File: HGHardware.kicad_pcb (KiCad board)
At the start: 2 copper layers, 220 x 60 mm, 109 parts, among them J1 Conn_01x04_Male, J2 SWD Conn, J3 USB_C_Receptacle_USB2.0, Q1 MMBTA42, Q2 FDS2672CT, SW1 SW_Push, SW2 SW_SPST, SW3 SW_Push, U1 STM32L433CBTx, U2 HV507PG-G-MyKiCadLib, U3 ESP-12S, U4 W25Q32FWSSIG, U5 UCC3803, U7 TXS0104EPWR, U9 AOZ1031, Y1 8MHz, Y2 8MHz

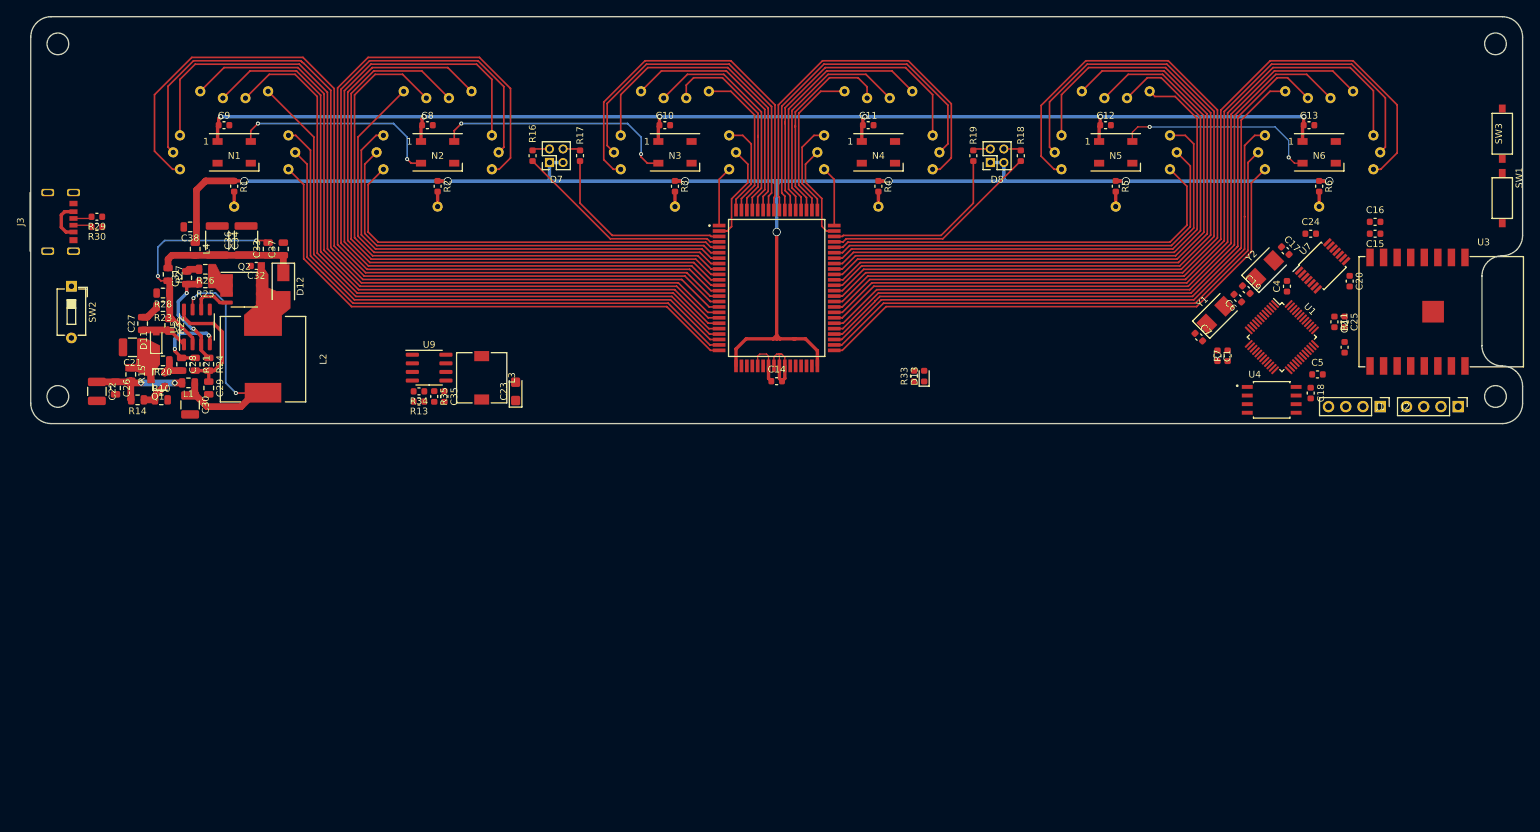
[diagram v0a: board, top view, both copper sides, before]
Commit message: 20210306完善原理图，升压模块将单独使用
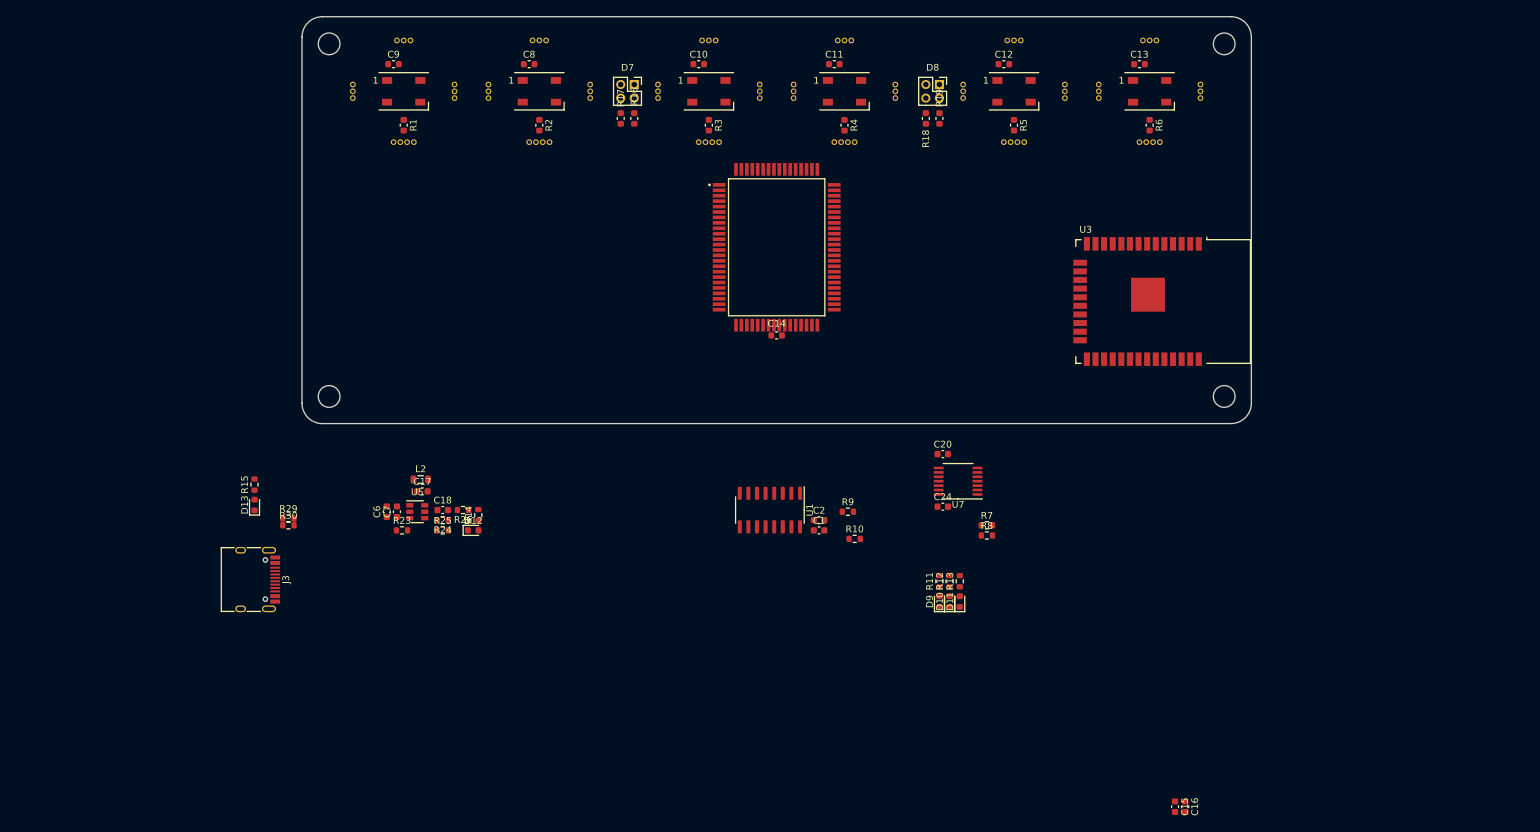
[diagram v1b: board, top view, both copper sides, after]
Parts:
- removed C19: 20pF, Capacitor_SMD:C_0603_1608Metric
- removed C21: 47uF 16v, Capacitor_SMD:C_1210_3225Metric
- removed C22, C30: 100uF 16v, Capacitor_SMD:C_1210_3225Metric
- removed C23: 10uF, Capacitor_Tantalum_SMD:CP_EIA-3216-18_Kemet-A
- removed C25, C35: 100nF, Capacitor_SMD:C_0603_1608Metric
- removed C26: 0.1uF, Capacitor_SMD:C_0805_2012Metric
- removed C27: 220pF, Capacitor_SMD:C_0805_2012Metric
- removed C28: 430pF, Capacitor_SMD:C_0805_2012Metric
- removed C29: 0.1uF 16v, Capacitor_SMD:C_0805_2012Metric
- removed C31: 1nF, Capacitor_SMD:C_0805_2012Metric
- removed C32: 560pF 250v, Capacitor_SMD:C_0603_1608Metric
- removed C33: 100pF 250v, Capacitor_SMD:C_0805_2012Metric
- removed C34, C36: 1uF 250v, Capacitor_SMD:C_1812_4532Metric
- removed C37, C38: 0.1uF 250v, Capacitor_SMD:C_0805_2012Metric
- removed C4, C5: C, Capacitor_SMD:C_0603_1608Metric
- removed J1: Conn_01x04_Male, Connector_PinHeader_2.54mm:PinHeader_1x04_P2.54mm_Vertical
- removed J2: SWD Conn, Connector_PinHeader_2.54mm:PinHeader_1x04_P2.54mm_Vertical
- removed L1, L4: 60ohm 100Mhz, Resistor_SMD:R_0805_2012Metric
- removed L3: 4.7uH, Inductor_SMD:L_7.3x7.3_H3.5
- removed Q1: MMBTA42, Package_TO_SOT_SMD:SOT-23
- removed Q2: FDS2672CT, Package_SO:SO-8_3.9x4.9mm_P1.27mm
- removed R20: 100k, Resistor_SMD:R_0805_2012Metric
- removed R21: 60.4k, Resistor_SMD:R_0805_2012Metric
- removed R22: N.U., Resistor_SMD:R_0805_2012Metric
- removed R27: 634k, Resistor_SMD:R_0805_2012Metric
- removed R28: 7.68k, Resistor_SMD:R_0805_2012Metric
- removed R33: 1KO, Resistor_SMD:R_0603_1608Metric
- removed R34: 10KO, Resistor_SMD:R_0603_1608Metric
- removed R35: 1.5KO, Resistor_SMD:R_0603_1608Metric
- removed SW1, SW3: SW_Push, HGHardware:MyButton
- removed SW2: SW_SPST, Button_Switch_THT:SW_DIP_SPSTx01_Slide_6.7x4.1mm_W7.62mm_P2.54mm_LowProfile
- removed U4: W25Q32FWSSIG, SOIC127P790X216-8N:SOIC127P790X216-8N
- removed U9: AOZ1031, Package_SO:SOIC-8_3.9x4.9mm_P1.27mm
- removed Y1, Y2: 8MHz, Crystal:Crystal_SMD_5032-2Pin_5.0x3.2mm
- added D10: BLUE, LED_SMD:LED_0603_1608Metric, F.Cu at (105.5, 66.2)
- added D9: GREEN, LED_SMD:LED_0603_1608Metric, F.Cu at (104.0, 66.2)
- added R12: 1KΩ, Resistor_SMD:R_0603_1608Metric, F.Cu at (105.5, 63.2)
- added R8: 120Ω, Resistor_SMD:R_0603_1608Metric, F.Cu at (111.0, 56.5)
- added R9: 10KΩ, Resistor_SMD:R_0603_1608Metric, F.Cu at (90.5, 53.0)
- C1: value 100nF -> 10uF
- C15: value 10uF -> 100uF
- C17, C7: value 20pF -> 100nF
- C18: value 100nF -> 22uF
- C2: value C -> 100nF
- C6: value 20pF -> 22uF
- D1: value WS2812C -> WS2812B×6
- D11: value BAT54 -> RED; footprint Diode_SMD:D_SOD-323_HandSoldering -> LED_SMD:LED_0603_1608Metric
- D12: value ES1D -> RED; footprint Diode_SMD:D_SMA -> LED_SMD:LED_0603_1608Metric
- D13: value LED -> RED
- D2, D3: value WS2812C -> WS2812B-2020
- J3: footprint HGHardware:USB TypeC 6P Horizontal -> Connector_USB:USB_C_Receptacle_HRO_TYPE-C-31-M-12
- L2: value 33uH -> 2.2uH; footprint Inductor_SMD:L_12x12mm_H4.5mm -> Inductor_SMD:L_0805_2012Metric
- N6: value NixieTube -> NixieTube×6
- R1, R2, R3, R4, R5, R6: value 33KO -> 33KΩ
- R10, R25: value 1k -> 10KΩ; footprint Resistor_SMD:R_0805_2012Metric -> Resistor_SMD:R_0603_1608Metric
- R11: value 10KO -> 1KΩ
- R13: value 31.1KO -> 1KΩ
- R14: value 100k -> 1KΩ; footprint Resistor_SMD:R_0805_2012Metric -> Resistor_SMD:R_0603_1608Metric
- R15: value 2k -> 1KΩ; footprint Resistor_SMD:R_0805_2012Metric -> Resistor_SMD:R_0603_1608Metric
- R17: value 510KO -> 510KΩ
- R23: value 0 Ohm -> 100KΩ; footprint Resistor_SMD:R_0805_2012Metric -> Resistor_SMD:R_0603_1608Metric
- R24: value 4.12k -> 30KΩ; footprint Resistor_SMD:R_0805_2012Metric -> Resistor_SMD:R_0603_1608Metric
- R26: value 0.1 1/2W -> 0Ω; footprint Resistor_SMD:R_0805_2012Metric -> Resistor_SMD:R_0603_1608Metric
- R29, R30: value 5.1K -> 5.1KΩ
- R7: value 10KO -> 120Ω
- U1: value STM32L433CBTx -> CH340C; footprint Package_QFP:LQFP-48_7x7mm_P0.5mm -> Package_SO:SOIC-16_3.9x9.9mm_P1.27mm
- U2: value HV507PG-G-MyKiCadLib -> HV507PG-G
- U3: value ESP-12S -> ESP32-WROOM-32; footprint ESP-12S:ESP-12S -> RF_Module:ESP32-WROOM-32
- U5: value UCC3803 -> TPS563201DDCR; footprint Package_SO:SO-8_3.9x4.9mm_P1.27mm -> Package_TO_SOT_SMD:SOT-23-6
- moved C17 132.1 mm to (27.8, 50.0), turned to 0 degrees
- moved C6 129.4 mm to (22.5, 53.0), turned to 90 degrees
- moved C18 129.2 mm to (30.8, 52.8), turned to 0 degrees
- moved D11 124.6 mm to (107.0, 66.2)
- moved C7 121.0 mm to (24.0, 53.0), turned to 90 degrees
- moved R10 104.3 mm to (91.5, 57.0)
- moved D13 100.6 mm to (3.00, 52.0)
- moved C16 90.7 mm to (140.2, 96.5), turned to 270 degrees
- moved C15 89.5 mm to (138.8, 96.5), turned to 270 degrees
- moved R13 84.0 mm to (107.0, 63.2), turned to 90 degrees
- moved C2 81.6 mm to (86.2, 54.2), turned to 0 degrees
- moved U1 79.7 mm to (79.0, 52.8), turned to 270 degrees
- moved R11 69.7 mm to (104.0, 63.2), turned to 90 degrees
- moved C24 67.6 mm to (104.5, 52.2), turned to 0 degrees
- moved C20 65.2 mm to (104.5, 44.5), turned to 0 degrees
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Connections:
- C1 pad 1: /NRST -> +3V3
- C1 pad 2: GND -> GNDD
- C10 pad 2: GND -> GNDD
- C11 pad 2: GND -> GNDD
- C12 pad 2: GND -> GNDD
- C13 pad 2: GND -> GNDD
- C14 pad 1: GND -> GNDD
- C15 pad 2: GND -> GNDD
- C16 pad 2: GND -> GNDD
- C17 pad 2: GND -> Net-(C17-Pad2)
- C18 pad 1: GND -> GNDD
- C18 pad 2: +3V3 -> Net-(C18-Pad2)
- C2 pad 2: GND -> GNDD
- C20 pad 2: GND -> GNDD
- C24 pad 2: GND -> GNDD
- C6 pad 1: Net-(C6-Pad1) -> +5V
- C7 pad 1: Net-(C7-Pad1) -> +5V
- C8 pad 2: GND -> GNDD
- C9 pad 2: GND -> GNDD
- D1 pad 3: GND -> GNDD
- D11 pad 1: Net-(C21-Pad1) -> Net-(D11-Pad1)
- D11 pad 2: Net-(C27-Pad1) -> Net-(D11-Pad2)
- D12 pad 1: Net-(C33-Pad1) -> GNDD
- D12 pad 2: Net-(C32-Pad1) -> Net-(D12-Pad2)
- D13 pad 1: Net-(D13-Pad1) -> GNDD
- D2 pad 3: GND -> GNDD
- D3 pad 3: GND -> GNDD
- D4 pad 3: GND -> GNDD
- D5 pad 3: GND -> GNDD
- D6 pad 2: (no net) -> Net-(D6-Pad2)
- D6 pad 3: GND -> GNDD
- L2 pad 1: Net-(C32-Pad1) -> Net-(C17-Pad1)
- L2 pad 2: Net-(C30-Pad1) -> Net-(C18-Pad2)
- R10 pad 1: Net-(Q1-Pad1) -> Net-(Q3-Pad2)
- R10 pad 2: /VPP_EN -> Net-(Q1-Pad1)
- R11 pad 1: /BOOT0 -> Net-(D9-Pad2)
- R11 pad 2: GND -> +3V3
- R13 pad 1: +3V3 -> Net-(D11-Pad2)
- R13 pad 2: Net-(R13-Pad2) -> +3V3
- R14 pad 1: Net-(Q1-Pad1) -> Net-(D12-Pad2)
- R14 pad 2: +5V -> +3V3
- R15 pad 1: Net-(C21-Pad1) -> Net-(D13-Pad2)
- R23 pad 1: Net-(C33-Pad2) -> +5V
- R23 pad 2: Net-(C27-Pad2) -> Net-(R23-Pad2)
- R24 pad 1: Net-(C31-Pad1) -> Net-(C18-Pad2)
- R24 pad 2: Net-(C29-Pad1) -> Net-(R24-Pad2)
- R25 pad 1: Net-(Q2-Pad1) -> Net-(R24-Pad2)
- R25 pad 2: Net-(C31-Pad1) -> GND
- R26 pad 1: Net-(Q2-Pad1) -> +3V3
- R26 pad 2: GND -> Net-(C18-Pad2)
- R7 pad 1: /NRST -> /CH340_TXD
- R7 pad 2: +3V3 -> Net-(R7-Pad2)
- U1 pad 1: +3V3 -> GNDD
- U1 pad 10: /WKP1 -> Net-(U1-Pad10)
- U1 pad 11: Net-(D13-Pad1) -> Net-(U1-Pad11)
- U1 pad 12: (no net) -> Net-(U1-Pad12)
- U1 pad 13: /VPP_EN -> Net-(Q3-Pad1)
- U1 pad 14: (no net) -> Net-(Q1-Pad1)
- U1 pad 15: (no net) -> Net-(U1-Pad15)
- U1 pad 16: /QSPI_IO3 -> +3V3
- U1 pad 2: (no net) -> Net-(R7-Pad2)
- U1 pad 3: Net-(C17-Pad1) -> Net-(R8-Pad2)
- U1 pad 4: Net-(C19-Pad1) -> +3V3
- U1 pad 5: Net-(C6-Pad1) -> /USB_D+
- U1 pad 6: Net-(C7-Pad1) -> /USB_D-
- U1 pad 7: /NRST -> Net-(U1-Pad7)
- U1 pad 8: GND -> Net-(U1-Pad8)
- U1 pad 9: +3V3 -> Net-(U1-Pad9)
- U2 pad 30: GND -> GNDD
- U2 pad 32: GND -> GNDD
- U2 pad 33: GND -> GNDD
- U2 pad 39: (no net) -> Net-(U2-Pad39)
- U3 pad 1: (no net) -> GNDD
- U3 pad 10: (no net) -> Net-(U3-Pad10)
- U3 pad 11: (no net) -> Net-(U3-Pad11)
- U3 pad 12: (no net) -> Net-(U3-Pad12)
- U3 pad 13: (no net) -> Net-(U3-Pad13)
- U3 pad 14: (no net) -> Net-(U3-Pad14)
- U3 pad 15: /UART1_TX -> GNDD
- U3 pad 16: /UART1_RX -> Net-(U3-Pad16)
- U3 pad 2: (no net) -> +3V3
- U3 pad 3: (no net) -> /ESP32_EN
- U3 pad 4: (no net) -> Net-(U3-Pad4)
- U3 pad 5: /WKP1 -> Net-(U3-Pad5)
- U3 pad 6: /NRST -> Net-(U3-Pad6)
- U3 pad 7: /BOOT0 -> Net-(U3-Pad7)
- U3 pad 8: +3V3 -> Net-(U3-Pad8)
- U3 pad 9: GND -> Net-(U3-Pad9)
- U5 pad 1: Net-(C27-Pad1) -> GND
- U5 pad 2: Net-(C33-Pad2) -> Net-(C17-Pad1)
- U5 pad 3: Net-(C31-Pad1) -> +5V
- U5 pad 4: Net-(C28-Pad1) -> Net-(R24-Pad2)
- U5 pad 5: GND -> Net-(R23-Pad2)
- U5 pad 6: Net-(Q2-Pad4) -> Net-(C17-Pad2)
- U7 pad 6: (no net) -> Net-(U7-Pad6)
- U7 pad 7: GND -> GNDD
- U7 pad 9: (no net) -> Net-(U7-Pad9)
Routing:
- net VPP: track 238.1 -> 0.00 mm, vias 7 -> 0
- net +5V: track 205.2 -> 0.00 mm, vias 8 -> 0
- net /N10: track 127.2 -> 0.00 mm
- net /N21: track 125.5 -> 0.00 mm
- net /N61: track 123.1 -> 0.00 mm
- net /N50: track 121.9 -> 0.00 mm
- net /N19: track 121.5 -> 0.00 mm
- net /N22: track 118.7 -> 0.00 mm
- net /N62: track 117.7 -> 0.00 mm
- net /N18: track 117.4 -> 0.00 mm
- net /N59: track 115.0 -> 0.00 mm
- net /N63: track 113.6 -> 0.00 mm
- net /N23: track 112.7 -> 0.00 mm
- net /N58: track 109.0 -> 0.00 mm
- net /N17: track 106.8 -> 0.00 mm
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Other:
- board size 220 x 60 mm -> 140 x 60 mm

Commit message: 犹豫不决ing
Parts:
- removed the C10 at (68.5, -13.0)
- removed the C15 at (138.8, 96.5)
- removed the C6 at (22.5, 53.0)
- removed the D6 at (25.0, -9.00)
- removed L2: 2.2uH, Inductor_SMD:L_0805_2012Metric
- removed the R1 at (25.0, -4.00)
- removed the R23 at (24.8, 55.8)
- removed the R26 at (33.8, 52.8)
- removed R30: 5.1KΩ, Resistor_SMD:R_0603_1608Metric
- added C1: 100uF, Capacitor_SMD:C_0603_1608Metric, F.Cu at (108.3, 73.3)
- added C13: 10uF, Capacitor_SMD:C_0603_1608Metric, F.Cu at (134.5, 56.1)
- added C14: 100nF, Capacitor_SMD:C_0603_1608Metric, F.Cu at (136.0, 56.1)
- added C2: 100nF, Capacitor_SMD:C_0603_1608Metric, F.Cu at (109.8, 73.3)
- added C3: 22uF, Capacitor_SMD:C_0603_1608Metric, F.Cu at (11.8, 28.7)
- added C4: 100nF, Capacitor_SMD:C_0603_1608Metric, F.Cu at (11.8, 30.2)
- added C8: C, Capacitor_SMD:C_0603_1608Metric, F.Cu at (58.2, 26.6)
- added D13: WS2812C, LED_SMD:LED_WS2812B_PLCC4_5.0x5.0mm_P3.2mm, F.Cu at (30.0, -9.00)
- added J1: USB_C_Receptacle_USB2.0, Connector_USB:USB_C_Receptacle_HRO_TYPE-C-31-M-12, F.Cu at (13.0, 14.9)
- added L1: 2.2uH, Inductor_SMD:L_Taiyo-Yuden_MD-4040, F.Cu at (16.3, 24.2)
- added Q1: S8050, Package_TO_SOT_SMD:SOT-23, F.Cu at (30.3, 15.7)
- added Q2: S8050, Package_TO_SOT_SMD:SOT-23, F.Cu at (30.3, 24.4)
- added Q3: S8050, Package_TO_SOT_SMD:SOT-23, F.Cu at (30.3, 20.9)
- added R13: 10KΩ, Resistor_SMD:R_0603_1608Metric, F.Cu at (28.5, 18.3)
- added R2: 5.1KΩ, Resistor_SMD:R_0603_1608Metric, F.Cu at (15.5, 21.1)
- added R22: 33KΩ, Resistor_SMD:R_0603_1608Metric, F.Cu at (70.2, -18.0)
- added R4: NC, Resistor_SMD:R_0603_1608Metric, F.Cu at (60.3, 28.9)
- added R9: 33KΩ, Resistor_SMD:R_0603_1608Metric, F.Cu at (29.2, -18.0)
- added U6: HV507PG-G, HGHardware:QFP80P2390X1790X340-80N, F.Cu at (80.0, 12.0)
- added Y1: 32.738kHz, Crystal:Crystal_SMD_2012-2Pin_2.0x1.2mm, F.Cu at (60.3, 27.2)
- C16, C17, C7: value 100nF -> C
- C9: value C -> 100nF
- J3: value USB_C_Receptacle_USB2.0 -> Conn_01x06; footprint Connector_USB:USB_C_Receptacle_HRO_TYPE-C-31-M-12 -> Connector_PinHeader_2.54mm:PinHeader_1x06_P2.54mm_Vertical
- R3: value 33KΩ -> 100KΩ
- U1: value CH340C -> ESP32-WROOM-32; footprint Package_SO:SOIC-16_3.9x9.9mm_P1.27mm -> RF_Module:ESP32-WROOM-32
- U2: value HV507PG-G -> ES8388; footprint QFP80P2390X1790X340-80N:QFP80P2390X1790X340-80N -> Package_DFN_QFN:QFN-28-1EP_4x4mm_P0.4mm_EP2.4x2.4mm_ThermalVias
- U3: value ESP32-WROOM-32 -> CH340K; footprint RF_Module:ESP32-WROOM-32 -> Package_SO:SSOP-10_3.9x4.9mm_P1.00mm
- moved C16 156.5 mm to (28.5, -13.0), turned to 0 degrees
- moved J3 112.0 mm to (112.7, 80.2), turned to 90 degrees
- moved U3 111.8 mm to (22.2, 18.0), turned to 0 degrees
- moved D8 90.1 mm to (22.5, 35.0), turned to 270 degrees
- moved R17 88.2 mm to (22.5, 38.0), turned to 270 degrees
- moved D7 87.3 mm to (24.0, 35.0), turned to 270 degrees
- moved R16 85.3 mm to (24.0, 38.0), turned to 270 degrees
- moved R5 85.2 mm to (30.5, 27.0), turned to 180 degrees
- moved R6 85.2 mm to (30.5, 28.5), turned to 180 degrees
- moved D6 84.5 mm to (25.5, 35.0), turned to 270 degrees
- moved R15 82.5 mm to (25.5, 38.0), turned to 270 degrees
- moved R12 75.8 mm to (27.7, 16.0), turned to 270 degrees
- moved C5 75.4 mm to (24.1, 12.9), turned to 180 degrees
- moved C17 74.1 mm to (67.5, -12.5), turned to 180 degrees
- moved C6 73.8 mm to (24.1, 14.4), turned to 180 degrees
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- renumbered C18 to C10, C20 to C11, C24 to C12, C8 to C15, C11 to C18, C12 to C19, C13 to C20, C14 to C21, C1 to C5, C2 to C6, D13 to D10, D5 to D11, D8 to D12, D7 to D5, D9 to D6, D10 to D7, D11 to D8, D12 to D9, R29 to R1, R9 to R11, R10 to R12, R2 to R14, R11 to R15, R12 to R16, R13 to R17, R14 to R18, R15 to R19, R17 to R20, R16 to R21, R18 to R23, R19 to R24, R4 to R25, R5 to R26, R6 to R27, R7 to R5, R8 to R6, R24 to R7, R25 to R8, U5 to U4, U7 to U5
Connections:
- net Net-(U1-Pad10) renamed /ESP32_IO25
- net Net-(U1-Pad11) renamed /ESP32_IO26
- net Net-(U1-Pad12) renamed /ESP32_IO27
- net Net-(U1-Pad7) renamed /ESP32_IO35
- C10 pad 2: Net-(C18-Pad2) -> +3V3
- C16 pad 1: +3V3 -> +5V
- C17 pad 1: Net-(C17-Pad1) -> +5V
- C17 pad 2: Net-(C17-Pad2) -> GNDD
- C7 pad 1: +5V -> GNDD
- C7 pad 2: GND -> /32K_XP
- C9 pad 1: +5V -> Net-(C9-Pad1)
- C9 pad 2: GNDD -> Net-(C9-Pad2)
- R1 pad 2: Net-(J3-PadA5) -> Net-(J1-PadA5)
- R11 pad 2: Net-(Q3-Pad1) -> /CH340_DTR
- R12 pad 2: Net-(Q1-Pad1) (its old number) -> /CH340_RTS
- R3 pad 1: VPP -> +5V
- R3 pad 2: Net-(N3-Pad1) -> Net-(R3-Pad2)
- R5 pad 2: Net-(R7-Pad2) (its old number) -> Net-(R5-Pad2)
- R6 pad 2: Net-(R8-Pad2) -> Net-(R6-Pad2)
- R7 pad 1: Net-(C18-Pad2) -> +3V3
- U1 pad 13: Net-(Q3-Pad1) -> /ESP32_IO14
- U1 pad 14: Net-(Q1-Pad1) (its old number) -> /ESP32_IO12
- U1 pad 15: Net-(U1-Pad15) -> GNDD
- U1 pad 16: +3V3 -> /ESP32_IO13
- U1 pad 2: Net-(R7-Pad2) (its old number) -> +3V3
- U1 pad 3: Net-(R8-Pad2) -> /ESP32_EN
- U1 pad 4: +3V3 -> Net-(U1-Pad4)
- U1 pad 5: /USB_D+ -> Net-(U1-Pad5)
- U1 pad 6: /USB_D- -> /ESP32_IO34
- U1 pad 8: Net-(U1-Pad8) -> /32K_XP
- U1 pad 9: Net-(U1-Pad9) -> /32K_XN
- U2 pad 1: /N31 -> Net-(U2-Pad1)
- U2 pad 10: /N25 -> Net-(U2-Pad10)
- U2 pad 11: /N24 -> Net-(U2-Pad11)
- U2 pad 12: /N23 -> Net-(U2-Pad12)
- U2 pad 13: /N22 -> Net-(U2-Pad13)
- U2 pad 14: /N21 -> Net-(U2-Pad14)
- U2 pad 15: /N10 -> Net-(U2-Pad15)
- U2 pad 16: /N19 -> Net-(U2-Pad16)
- U2 pad 17: /N18 -> Net-(U2-Pad17)
- U2 pad 18: /N17 -> Net-(U2-Pad18)
- U2 pad 19: /N16 -> Net-(U2-Pad19)
- U2 pad 2: /N32 -> Net-(U2-Pad2)
- U2 pad 20: /N15 -> Net-(U2-Pad20)
- U2 pad 21: /N14 -> Net-(U2-Pad21)
- U2 pad 22: /N13 -> Net-(U2-Pad22)
- U2 pad 23: /N12 -> Net-(U2-Pad23)
- U2 pad 24: /N11 -> Net-(U2-Pad24)
- U2 pad 25: VPP -> (no net)
- U2 pad 26: /HV_DIN_5V -> Net-(U2-Pad26)
- U2 pad 27: (no net) -> Net-(U2-Pad27)
- U2 pad 28: (no net) -> Net-(U2-Pad28)
- U2 pad 29: +5V -> Net-(U2-Pad29)
- U2 pad 3: /ND2 -> Net-(U2-Pad3)
- U2 pad 4: /ND1 -> Net-(U2-Pad4)
- U2 pad 5: /N20 -> Net-(U2-Pad5)
- U2 pad 6: /N29 -> Net-(U2-Pad6)
- U2 pad 7: /N28 -> Net-(U2-Pad7)
- U2 pad 8: /N27 -> Net-(U2-Pad8)
- U2 pad 9: /N26 -> (no net)
- U3 pad 1: GNDD -> /USB_D+
- U3 pad 10: Net-(U3-Pad10) -> +3V3
- U3 pad 2: +3V3 -> /USB_D-
- U3 pad 3: /ESP32_EN -> GNDD
- U3 pad 4: Net-(U3-Pad4) -> /CH340_DTR
- U3 pad 6: Net-(U3-Pad6) -> /CH340_RTS
- U3 pad 7: Net-(U3-Pad7) -> +3V3
- U3 pad 8: Net-(U3-Pad8) -> Net-(R5-Pad2)
- U3 pad 9: Net-(U3-Pad9) -> Net-(R6-Pad2)
- U4 pad 2: Net-(C17-Pad1) -> Net-(C9-Pad1)
- U4 pad 5: Net-(R23-Pad2) -> Net-(R3-Pad2)
- U4 pad 6: Net-(C17-Pad2) -> Net-(C9-Pad2)
